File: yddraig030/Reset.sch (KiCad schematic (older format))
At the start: 22 parts

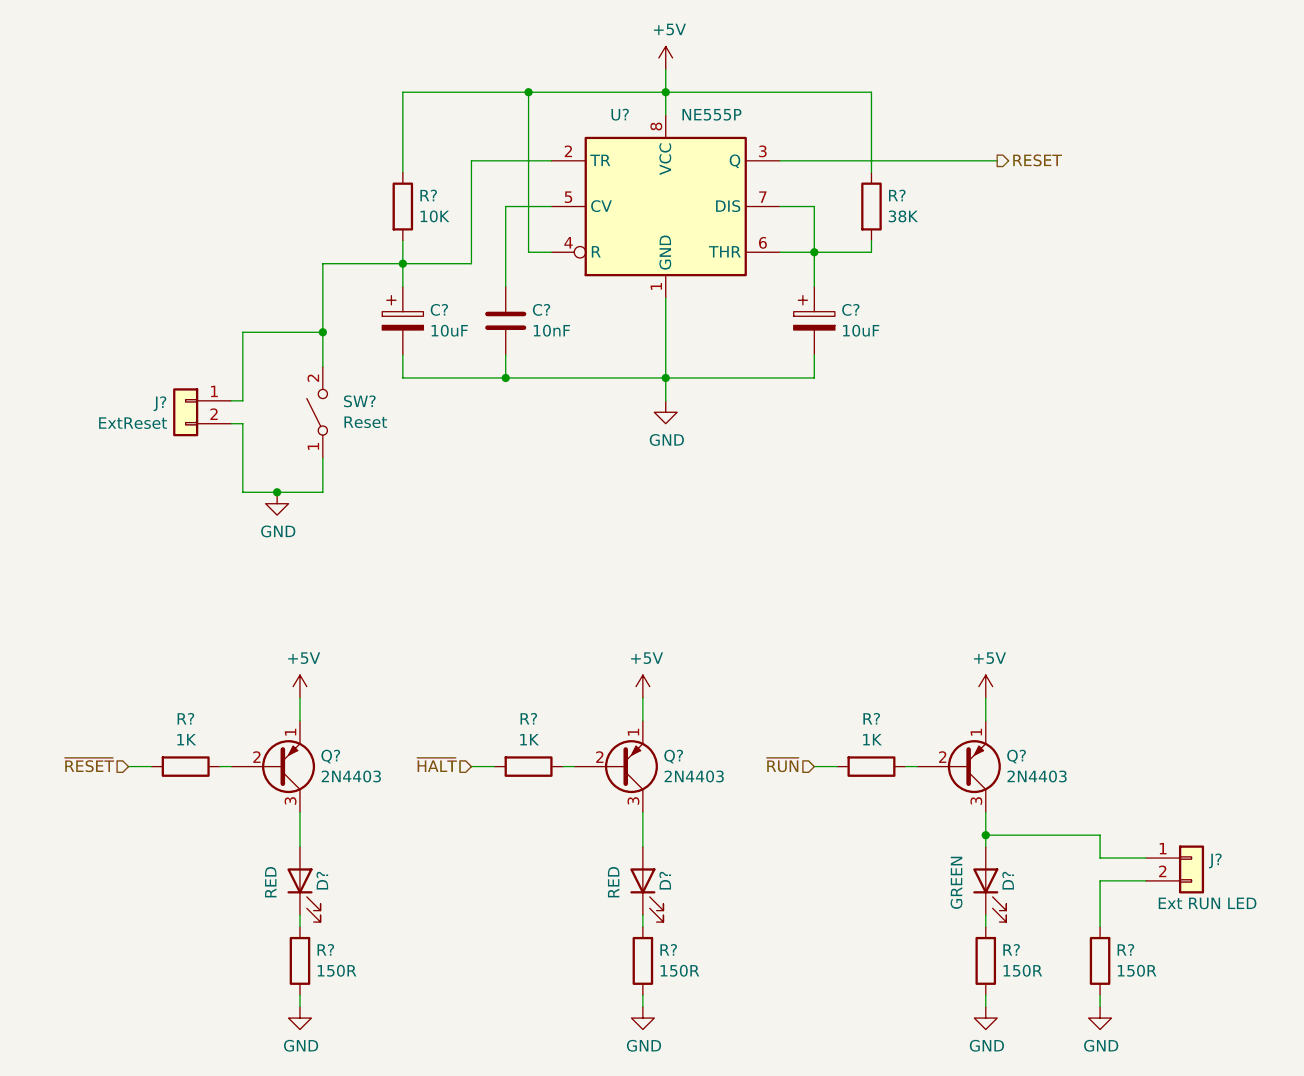
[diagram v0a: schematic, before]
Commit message: Changes to 6809 and 68030 schematics
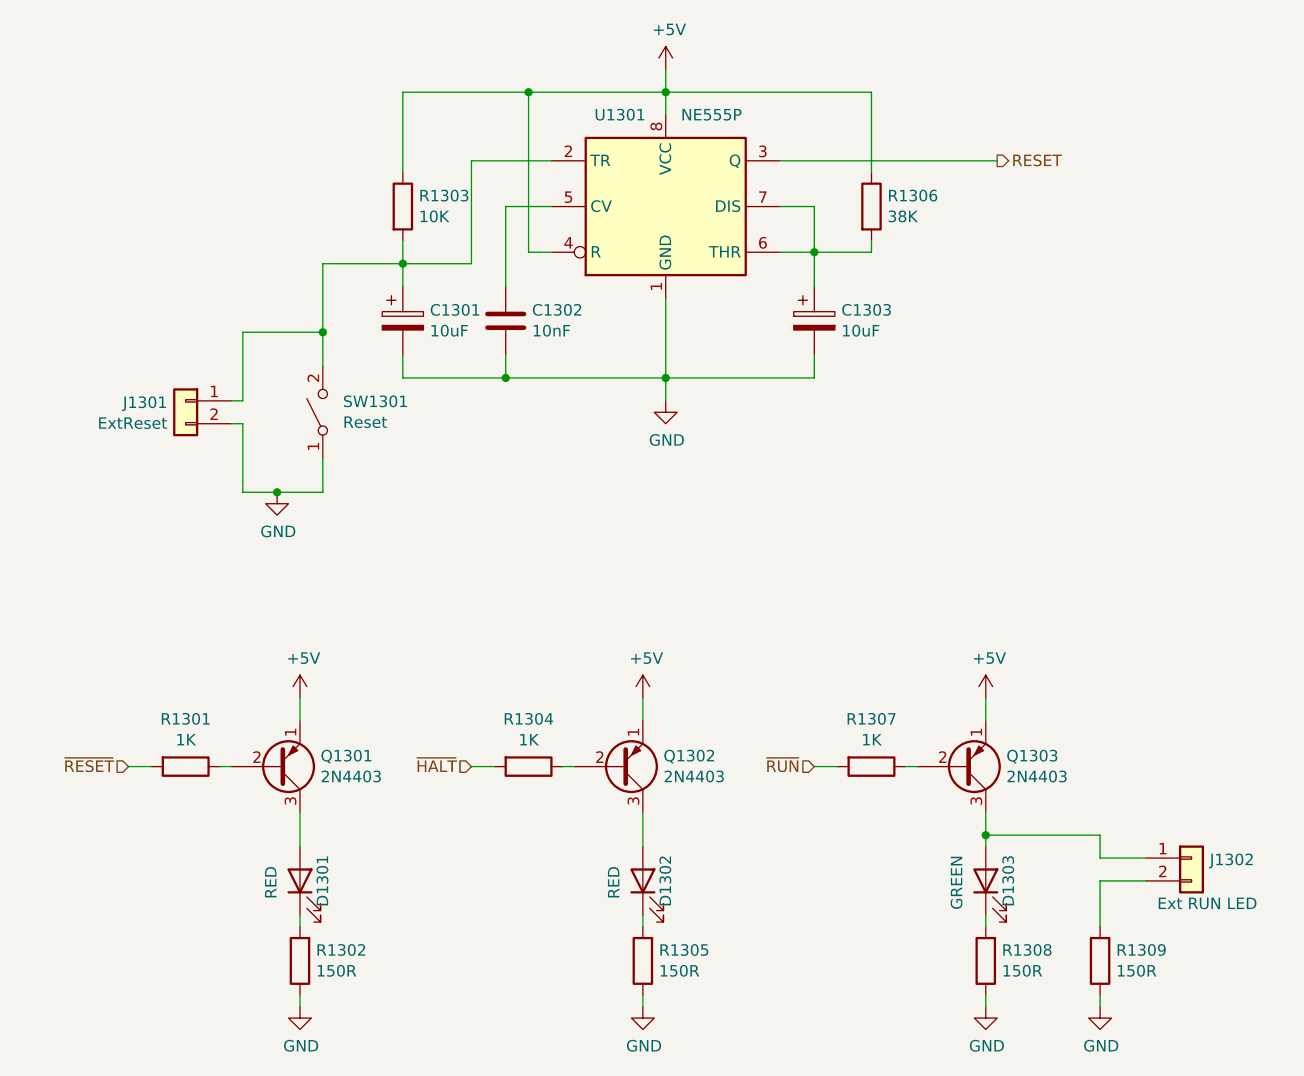
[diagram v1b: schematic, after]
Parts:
- gave numbers to parts that had none: 22
